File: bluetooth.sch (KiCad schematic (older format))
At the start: 4 parts

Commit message: Move some stuff around and add reset button to WT12
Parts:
- added SW?: SW_PUSH, symbol SW_PUSH
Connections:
- net VCC: now also SW?.2
- net W_RESET: now also SW?.1
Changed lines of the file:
@@
 $Descr A4 11693 8268
 encoding utf-8
-Sheet 4 5
+Sheet 4 6
 Title ""
 Date ""
@@
 Wire Wire Line
 	3650 5050 3950 5050
+$Comp
+L SW_PUSH SW?
+U 1 1 54E72241
+P 8650 4500
+F 0 "SW?" H 8800 4610 50  0000 C CNN
+F 1 "SW_PUSH" H 8650 4420 50  0000 C CNN
+F 2 "" H 8650 4500 60  0000 C CNN
+F 3 "" H 8650 4500 60  0000 C CNN
+	1    8650 4500
+	1    0    0    -1
+$EndComp
+Text GLabel 8250 4500 0    60   Input ~ 0
+W_RESET
+$Comp
+L VCC #PWR?
+U 1 1 54E7230E
+P 9150 4450
+F 0 "#PWR?" H 9150 4550 30  0001 C CNN
+F 1 "VCC" H 9150 4550 30  0000 C CNN
+F 2 "" H 9150 4450 60  0000 C CNN
+F 3 "" H 9150 4450 60  0000 C CNN
+	1    9150 4450
+	1    0    0    -1
+$EndComp
+Wire Wire Line
+	8250 4500 8350 4500
+Wire Wire Line
+	8950 4500 9150 4500
+Wire Wire Line
+	9150 4500 9150 4450
 $EndSCHEMATC

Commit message: Move Bluetooth wire assignment to front sheet
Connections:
- net PD2 renamed W_TXD
- net PD3 renamed W_RXD
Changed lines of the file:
@@
 	4950 2500 4950 3500
 Connection ~ 4950 3500
-Text GLabel 3950 4950 2    60   Input ~ 0
-PD2
-Text GLabel 3950 5050 2    60   Input ~ 0
-PD3
-Text GLabel 3650 4950 0    60   Input ~ 0
-W_TXD
-Text GLabel 3650 5050 0    60   Input ~ 0
-W_RXD
-Wire Wire Line
-	3650 4950 3950 4950
-Wire Wire Line
-	3650 5050 3950 5050
 $Comp
 L SW_PUSH SW?

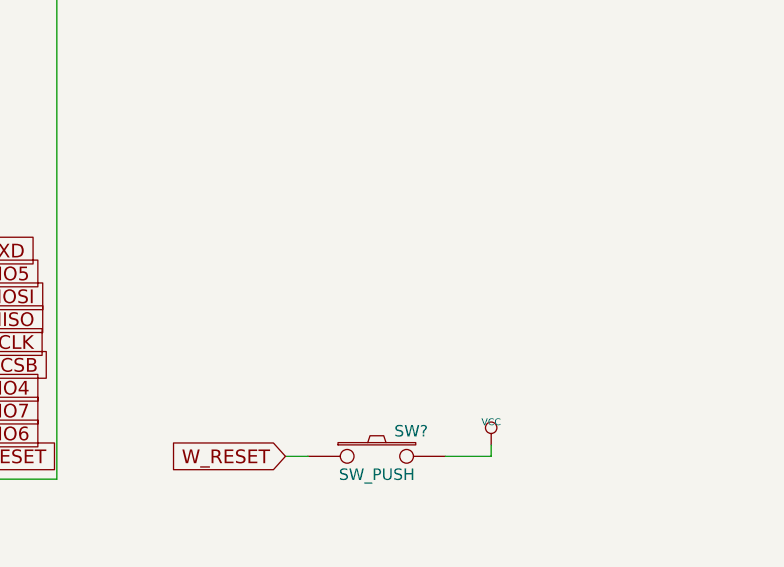
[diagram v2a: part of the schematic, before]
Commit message: Add PIO5 LED to WT12 circuit like the breakoutboard has
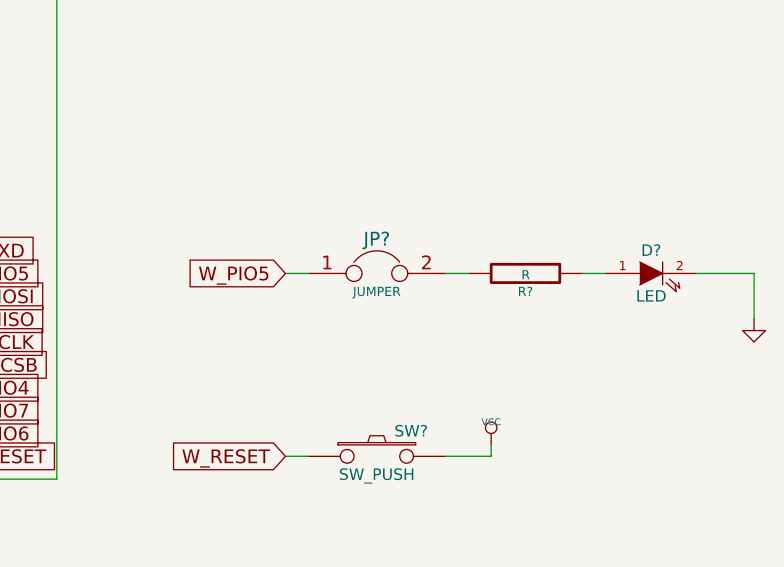
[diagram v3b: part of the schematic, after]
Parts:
- added D?: LED, symbol LED
- added JP?: JUMPER, symbol JUMPER
- added R?: R, symbol R
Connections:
- net GND: now also D?.2 (K)
- net W_PIO5: now also JP?.1
- new net: JP?.2, R?.2
- new net: D?.1 (A), R?.1
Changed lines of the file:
@@
 Wire Wire Line
 	9150 4500 9150 4450
+Text GLabel 8250 3700 0    60   Input ~ 0
+W_PIO5
+$Comp
+L JUMPER JP?
+U 1 1 54E9AF59
+P 8650 3700
+F 0 "JP?" H 8650 3850 60  0000 C CNN
+F 1 "JUMPER" H 8650 3620 40  0000 C CNN
+F 2 "" H 8650 3700 60  0000 C CNN
+F 3 "" H 8650 3700 60  0000 C CNN
+	1    8650 3700
+	1    0    0    -1
+$EndComp
+$Comp
+L R R?
+U 1 1 54E9AF94
+P 9300 3700
+F 0 "R?" V 9380 3700 40  0000 C CNN
+F 1 "R" V 9307 3701 40  0000 C CNN
+F 2 "" V 9230 3700 30  0000 C CNN
+F 3 "" H 9300 3700 30  0000 C CNN
+	1    9300 3700
+	0    1    1    0
+$EndComp
+$Comp
+L LED D?
+U 1 1 54E9AFFB
+P 9850 3700
+F 0 "D?" H 9850 3800 50  0000 C CNN
+F 1 "LED" H 9850 3600 50  0000 C CNN
+F 2 "" H 9850 3700 60  0000 C CNN
+F 3 "" H 9850 3700 60  0000 C CNN
+	1    9850 3700
+	1    0    0    -1
+$EndComp
+$Comp
+L GND #PWR?
+U 1 1 54E9B03C
+P 10300 3900
+F 0 "#PWR?" H 10300 3900 30  0001 C CNN
+F 1 "GND" H 10300 3830 30  0001 C CNN
+F 2 "" H 10300 3900 60  0000 C CNN
+F 3 "" H 10300 3900 60  0000 C CNN
+	1    10300 3900
+	1    0    0    -1
+$EndComp
+Wire Wire Line
+	10300 3900 10300 3700
+Wire Wire Line
+	10300 3700 10050 3700
+Wire Wire Line
+	9650 3700 9550 3700
+Wire Wire Line
+	9050 3700 8950 3700
+Wire Wire Line
+	8350 3700 8250 3700
 $EndSCHEMATC
